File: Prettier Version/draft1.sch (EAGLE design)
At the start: 12 parts, among them J2 CONN-51P-FPC-MOLEX, J4 DISPLAYPORT-SINK-MOLEX

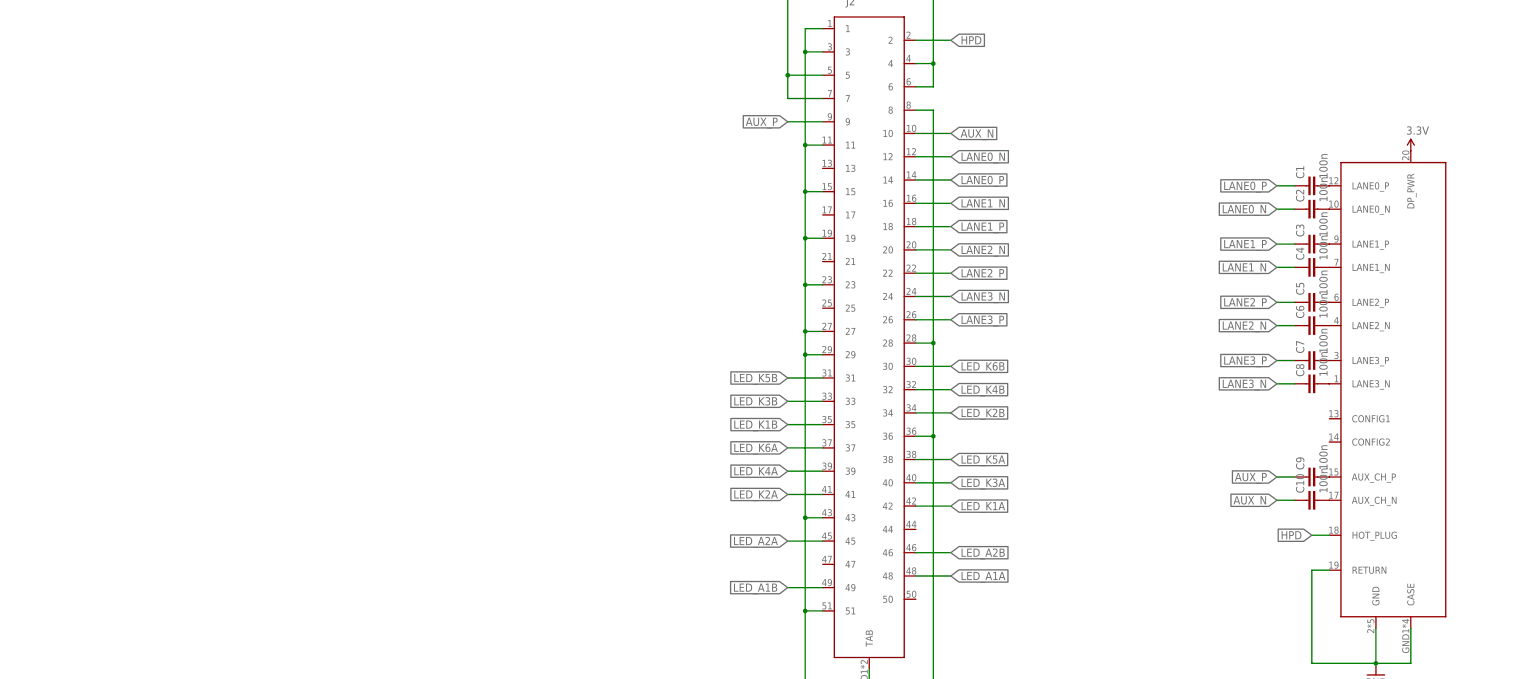
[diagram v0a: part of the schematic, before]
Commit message: Schematic work
Added LED control
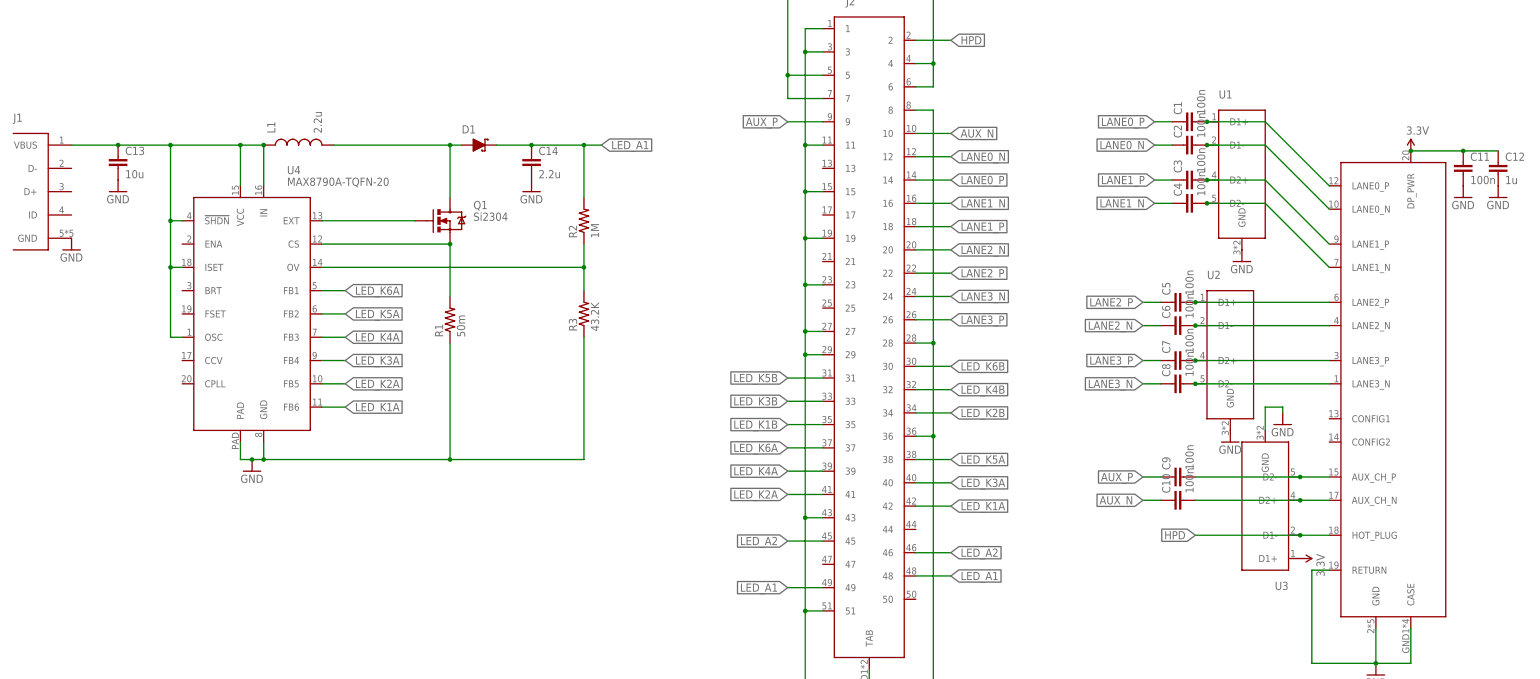
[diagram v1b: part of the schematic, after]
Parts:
- added C11: 100n, 00-EvaLibrary:C-EUC0805
- added C12: 1u, 00-EvaLibrary:C-EUC0805
- added C13: 10u, 00-EvaLibrary:C-EUC1206
- added C14: 2.2u, 00-EvaLibrary:C-EUC1206
- added D1: DB2W40300L, 00-EvaLibrary:DIODE-SCHOTTKY-MINI2-F3-B
- added J1: USB_MICRO_AB, 00-EvaLibrary:USB_MICRO_AB
- added L1: 2.2u, 00-EvaLibrary:INDUCTOR1210
- added Q1: Si2304, SparkFun-DiscreteSemi:MOSFET-NCHANNELSMD
- added R1: 50m, 00-EvaLibrary:R-US_MCS1632
- added R2: 1M, 00-EvaLibrary:R-US_R0603
- added R3: 43.2K, 00-EvaLibrary:R-US_R0603
- added U1, U2, U3: ESD-SUPPRESSOR-4-TPD4S010-DQA, 00-EvaLibrary:ESD-SUPPRESSOR-4-TPD4S010-DQA
- added U4: MAX8790A-TQFN-20, 00-EvaLibrary:MAX8790A-TQFN-20
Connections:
- removed net LED_A1A: J2.48
- removed net LED_A1B: J2.49
- removed net LED_A2A: J2.45
- removed net LED_A2B: J2.46
- new net LED_A1: C14.1, D1.K, J2.48, J2.49, R2.2
- new net LED_A2: J2.45, J2.46
- new net N$11: Q1.S, R1.2, U4.CS
- new net N$12: C13.1, J1.VBUS, L1.1, U4.!SHDN, U4.IN, U4.ISET, U4.OSC, U4.VCC
- new net N$13: Q1.G, U4.EXT
- new net N$14: D1.A, L1.2, Q1.D
- new net N$15: R2.1, R3.2, U4.OV
- net 3.3V: now also C11.1, C12.1, U3.D1+
- net GND: now also C11.2, C12.2, C13.2, C14.2, J1.GND, R1.1, R3.1, U1.GND, U2.GND, U3.GND, U4.GND, U4.PAD
- net HPD: now also U3.D1-
- net LED_K1A: now also U4.FB6
- net LED_K2A: now also U4.FB5
- net LED_K3A: now also U4.FB4
- net LED_K4A: now also U4.FB3
- net LED_K5A: now also U4.FB2
- net LED_K6A: now also U4.FB1
- net N$1: now also C4.2, J4.LANE1_N, U1.D2-; no longer C1.2, J4.LANE0_P
- net N$10: now also U3.D2+
- net N$2: now also C3.2, J4.LANE1_P, U1.D2+; no longer C2.2, J4.LANE0_N
- net N$3: now also C2.2, J4.LANE0_N, U1.D1-; no longer C3.2, J4.LANE1_P
- net N$4: now also C1.2, J4.LANE0_P, U1.D1+; no longer C4.2, J4.LANE1_N
- net N$5: now also U2.D1+
- net N$6: now also U2.D1-
- net N$7: now also U2.D2+
- net N$8: now also U2.D2-
- net N$9: now also U3.D2-
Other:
- moved on the sheet: C1, C10, C2, C3, C4, C5, C6, C7, C8, C9

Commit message: Prelim. PCB layout
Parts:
- removed J1: USB_MICRO_AB, 00-EvaLibrary:USB_MICRO_AB
- added C15, C18: 0.1u, 00-EvaLibrary:C-EUC0603
- added C16, C19, C20, C21: 1u, 00-EvaLibrary:C-EUC0603
- added C17: 2.2u, 00-EvaLibrary:C-EUC1206
- added D2: DB2W40300L, 00-EvaLibrary:DIODE-SCHOTTKY-MINI2-F3-B
- added ISP: AVR_SPI_PRG_6PTH, SparkFun-Connectors:AVR_SPI_PRG_6PTH
- added L2: 2.2u, 00-EvaLibrary:INDUCTOR1210
- added Q2: Si2304, SparkFun-DiscreteSemi:MOSFET-NCHANNELSMD
- added R10, R9: 22, 00-EvaLibrary:R-US_R0603
- added R11, R12: 4.7K, 00-EvaLibrary:R-US_R0603
- added R4, R8: 1.2K, 00-EvaLibrary:R-US_R0603
- added R5: 50m, 00-EvaLibrary:R-US_MCS1632
- added R6: 1M, 00-EvaLibrary:R-US_R0603
- added R7: 43.2K, 00-EvaLibrary:R-US_R0603
- added SERIAL: HEADER-6X1-961106-5500, 00-EvaLibrary:HEADER-6X1-961106-5500
- added TOUCH: HEADER-6X1-FPC-LOWER_CONTACT, 00-EvaLibrary:HEADER-6X1-FPC-LOWER_CONTACT
- added U5: MAX8790A-TQFN-20, 00-EvaLibrary:MAX8790A-TQFN-20
- added U6: ATMEGA32U4-QFN-44, 00-EvaLibrary:ATMEGA32U4-QFN-44
- added U7: TLV700DDC, 00-EvaLibrary:TLV700DDC
- added USB: USB_MICRO_AB, 00-EvaLibrary:USB_MICRO_AB
- renumbered J4 to DP
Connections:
- new net !RESET: ISP.5, U6.!RESET
- new net BRIGHTNESS1: U4.BRT
- new net BRIGHTNESS2: U5.BRT
- new net CTS: SERIAL.5, U6.PD5
- new net D+: R9.2, USB.D+
- new net D-: R10.2, USB.D-
- new net D3.3V: C21.1, R11.2, R12.2, TOUCH.5, U6.AVCC, U6.VCC, U7.VOUT
- new net INT: TOUCH.4, U6.PC7
- new net MISO: ISP.1, U6.PB3
- new net MOSI: ISP.4, U6.PB2
- new net N$16: R4.2, U4.CCV
- new net N$17: C15.1, R4.1
- new net N$18: D2.A, L2.2, Q2.D
- new net N$19: Q2.S, R5.2, U5.CS
- new net N$20: R6.1, R7.2, U5.OV
- new net N$21: R8.2, U5.CCV
- new net N$22: C18.1, R8.1
- new net N$23: R9.1, U6.D+
- new net N$24: R10.1, U6.D-
- new net N$25: C20.1, U6.UCAP
- new net RTS: SERIAL.1, U6.PB7
- new net RXD: SERIAL.3, U6.PD2
- new net SCL: R11.1, TOUCH.3, U6.PD0
- new net SCLK: ISP.3, U6.PB1
- new net SCREEN_!RESET: TOUCH.1, U6.PF6
- new net SDA: R12.1, TOUCH.2, U6.PD1
- new net TXD: SERIAL.2, U6.PD3
- new net VBUS: C13.1, C16.1, C19.1, ISP.2, L1.1, L2.1, SERIAL.4, U4.!SHDN, U4.FSET, U4.IN, U4.ISET, U4.OSC, U4.VCC, U5.!SHDN, U5.FSET, U5.IN, U5.ISET, U5.OSC, U5.VCC, U6.UVCC, U6.VBUS, U7.EN, U7.VIN, USB.VBUS
- net GND: now also C15.2, C16.2, C17.2, C18.2, C19.2, C20.2, C21.2, ISP.6, R5.1, R7.1, SERIAL.6, TOUCH.6, U4.ENA, U5.ENA, U5.GND, U5.PAD, U6.GND, U6.UGND, U7.GND, USB.GND; no longer J1.GND
- net LED_A2: now also C17.1, D2.K, R6.2
- net LED_K1B: now also U5.FB6
- net LED_K2B: now also U5.FB3
- net LED_K3A: now also U4.FB2; no longer U4.FB4
- net LED_K3B: now also U5.FB5
- net LED_K4A: now also U4.FB4; no longer U4.FB3
- net LED_K4B: now also U5.FB2
- net LED_K5A: now also U4.FB1; no longer U4.FB2
- net LED_K5B: now also U5.FB4
- net LED_K6A: now also U4.FB3; no longer U4.FB1
- net LED_K6B: now also U5.FB1
- net N$12: now also Q2.G, U5.EXT; no longer C13.1, J1.VBUS, L1.1, U4.!SHDN, U4.IN, U4.ISET, U4.OSC, U4.VCC
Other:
- moved on the sheet: C13

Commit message: Misc updates
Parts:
- added C22, C23: 18p, 00-EvaLibrary:C-EUC0603
- added X1: 16MHz, 00-EvaLibrary:XTAL-ABRACONABM3C
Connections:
- new net N$26: C22.1, U6.XTAL2, X1.1
- new net N$27: C23.1, U6.XTAL1, X1.2
- net GND: now also C22.2, C23.2, X1.CASE
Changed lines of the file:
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@@
 <part name="ISP" library="SparkFun-Connectors" deviceset="AVR_SPI_PRG_6" device="PTH"/>
 <part name="GND22" library="00-EvaLibrary" deviceset="GND" device=""/>
+<part name="X1" library="00-EvaLibrary" deviceset="XTAL-ABRACON" device="ABM3C" value="16MHz"/>
+<part name="GND23" library="00-EvaLibrary" deviceset="GND" device=""/>
+<part name="C22" library="00-EvaLibrary" deviceset="C-EU" device="C0603" value="18p"/>
+<part name="GND24" library="00-EvaLibrary" deviceset="GND" device=""/>
+<part name="C23" library="00-EvaLibrary" deviceset="C-EU" device="C0603" value="18p"/>
+<part name="GND25" library="00-EvaLibrary" deviceset="GND" device=""/>
 </parts>
 <sheets>
@@
 </instance>
 <instance part="GND22" gate="G$1" x="-358.14" y="29.21"/>
+<instance part="X1" gate="G$1" x="-228.6" y="6.35"/>
+<instance part="GND23" gate="G$1" x="-240.03" y="-3.81"/>
+<instance part="C22" gate="G$1" x="-240.03" y="3.81"/>
+<instance part="GND24" gate="G$1" x="-220.98" y="-3.81"/>
+<instance part="C23" gate="G$1" x="-220.98" y="3.81"/>
+<instance part="GND25" gate="G$1" x="-228.6" y="-2.54"/>
 </instances>
 <busses>
@@
 <pinref part="ISP" gate="G$1" pin="6"/>
 <pinref part="GND22" gate="G$1" pin="GND"/>
+</segment>
+<segment>
+<pinref part="GND23" gate="G$1" pin="GND"/>
+<pinref part="C22" gate="G$1" pin="2"/>
+</segment>
+<segment>
+<pinref part="GND24" gate="G$1" pin="GND"/>
+<pinref part="C23" gate="G$1" pin="2"/>
+</segment>
+<segment>
+<pinref part="X1" gate="G$1" pin="CASE"/>
+<pinref part="GND25" gate="G$1" pin="GND"/>
 </segment>
 </net>
@@
 </segment>
 </net>
+<net name="N$26" class="0">
+<segment>
+<pinref part="U6" gate="G$1" pin="XTAL2"/>
+<pinref part="X1" gate="G$1" pin="1"/>
+<wire x1="-245.11" y1="6.35" x2="-240.03" y2="6.35" width="0.1524" layer="91"/>
+<pinref part="C22" gate="G$1" pin="1"/>
+<wire x1="-240.03" y1="6.35" x2="-233.68" y2="6.35" width="0.1524" layer="91"/>
+<junction x="-240.03" y="6.35"/>
+</segment>
+</net>
+<net name="N$27" class="0">
+<segment>
+<pinref part="U6" gate="G$1" pin="XTAL1"/>
+<wire x1="-245.11" y1="11.43" x2="-220.98" y2="11.43" width="0.1524" layer="91"/>
+<wire x1="-220.98" y1="11.43" x2="-220.98" y2="6.35" width="0.1524" layer="91"/>
+<pinref part="X1" gate="G$1" pin="2"/>
+<wire x1="-220.98" y1="6.35" x2="-223.52" y2="6.35" width="0.1524" layer="91"/>
+<pinref part="C23" gate="G$1" pin="1"/>
+<junction x="-220.98" y="6.35"/>
+</segment>
+</net>

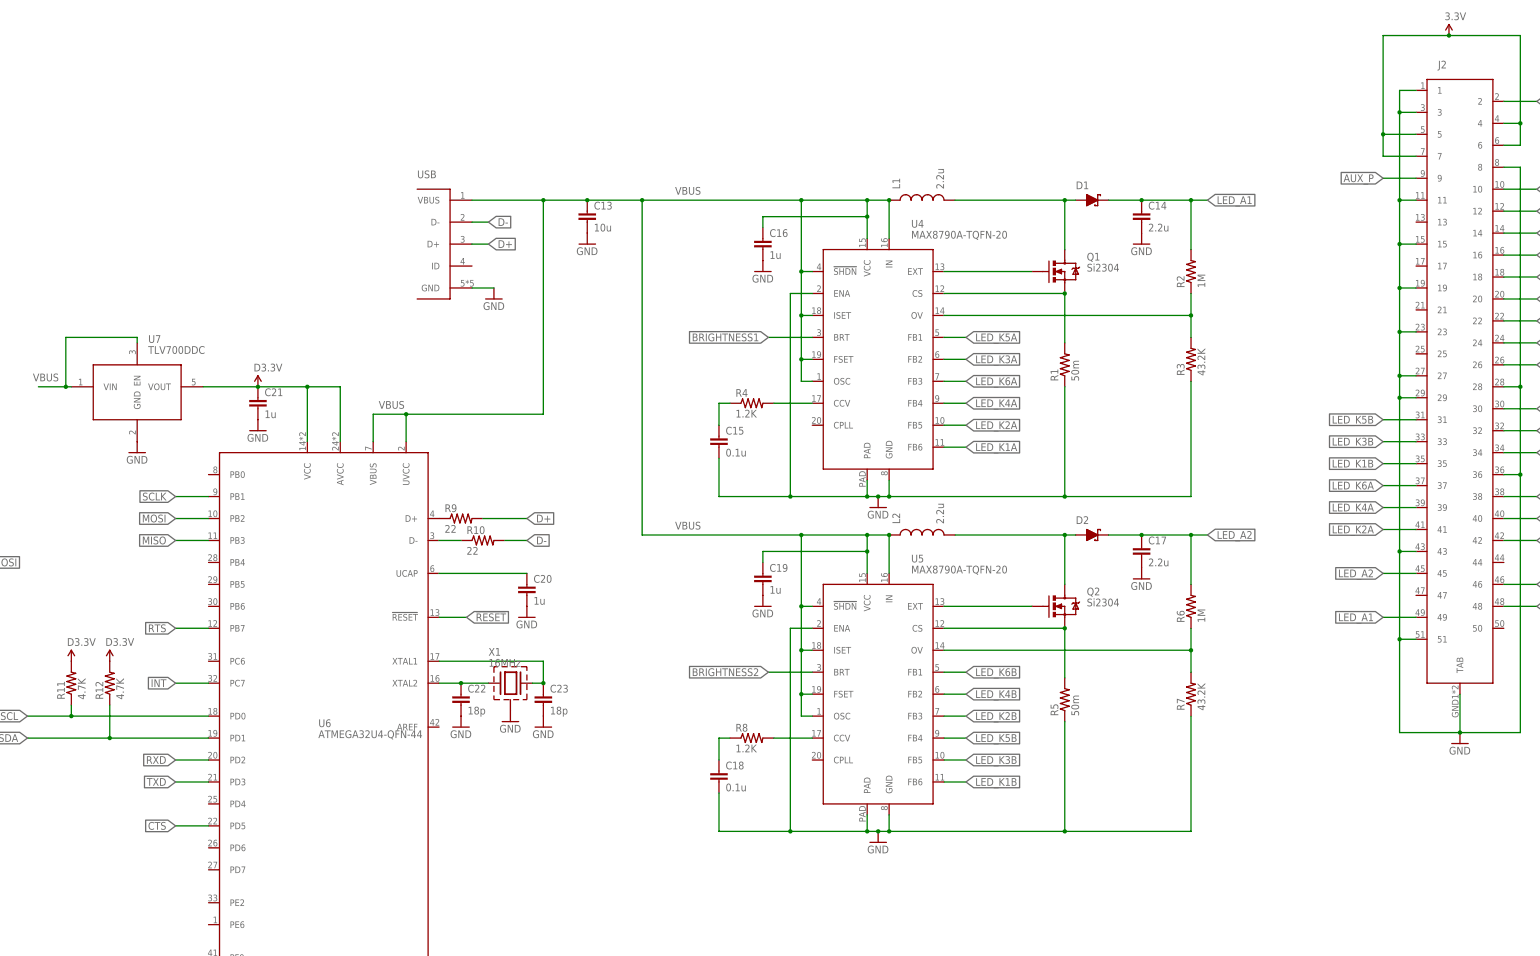
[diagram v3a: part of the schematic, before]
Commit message: Deleted PCB layout
Pending physical measurements
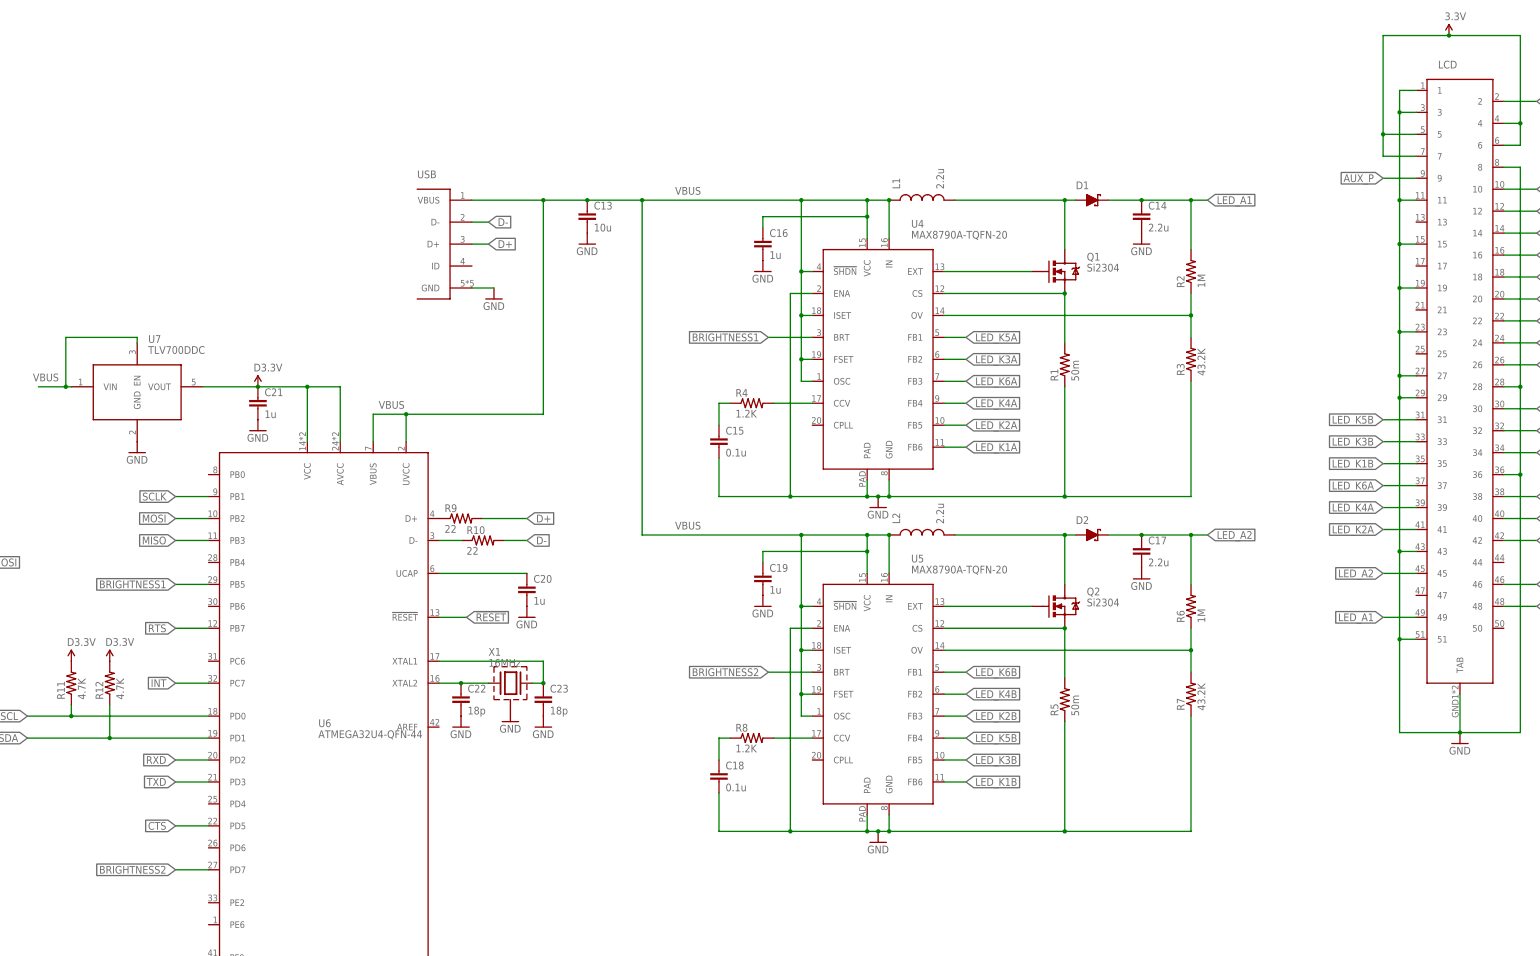
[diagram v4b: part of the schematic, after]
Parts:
- TOUCH: value HEADER-6X1-FPC-LOWER_CONTACT -> HEADER-6X1-FPC-DUAL_CONTACT; device 00-EvaLibrary:HEADER-6X1-FPC-LOWER_CONTACT -> 00-EvaLibrary:HEADER-6X1-FPC-DUAL_CONTACT
- renumbered J2 to LCD
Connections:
- net BRIGHTNESS1: now also U6.PB5
- net BRIGHTNESS2: now also U6.PD7
